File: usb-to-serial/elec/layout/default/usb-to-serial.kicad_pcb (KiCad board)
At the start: 2 copper layers, 225.7 x 100.8 mm, 0 parts

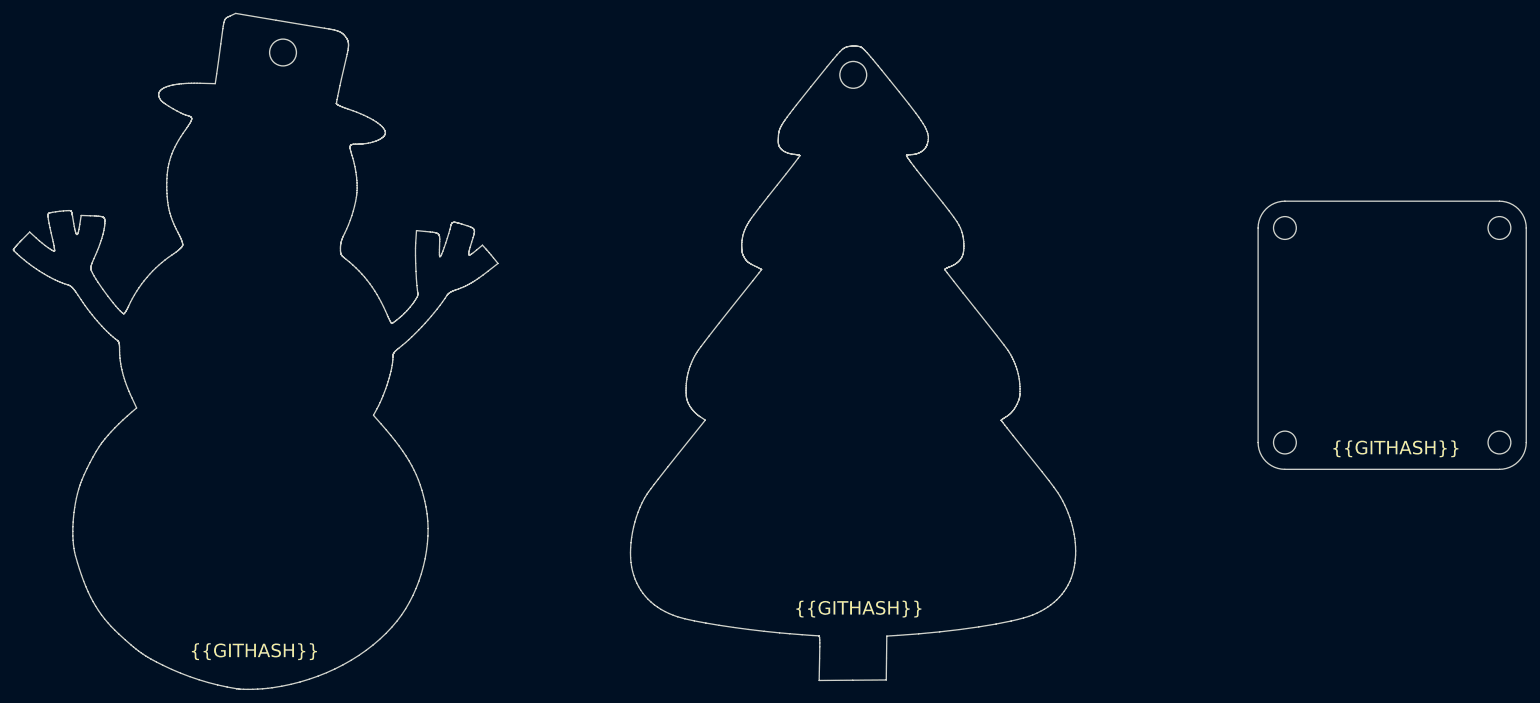
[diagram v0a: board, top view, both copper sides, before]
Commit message: updated usb to serial dev module, connected traces
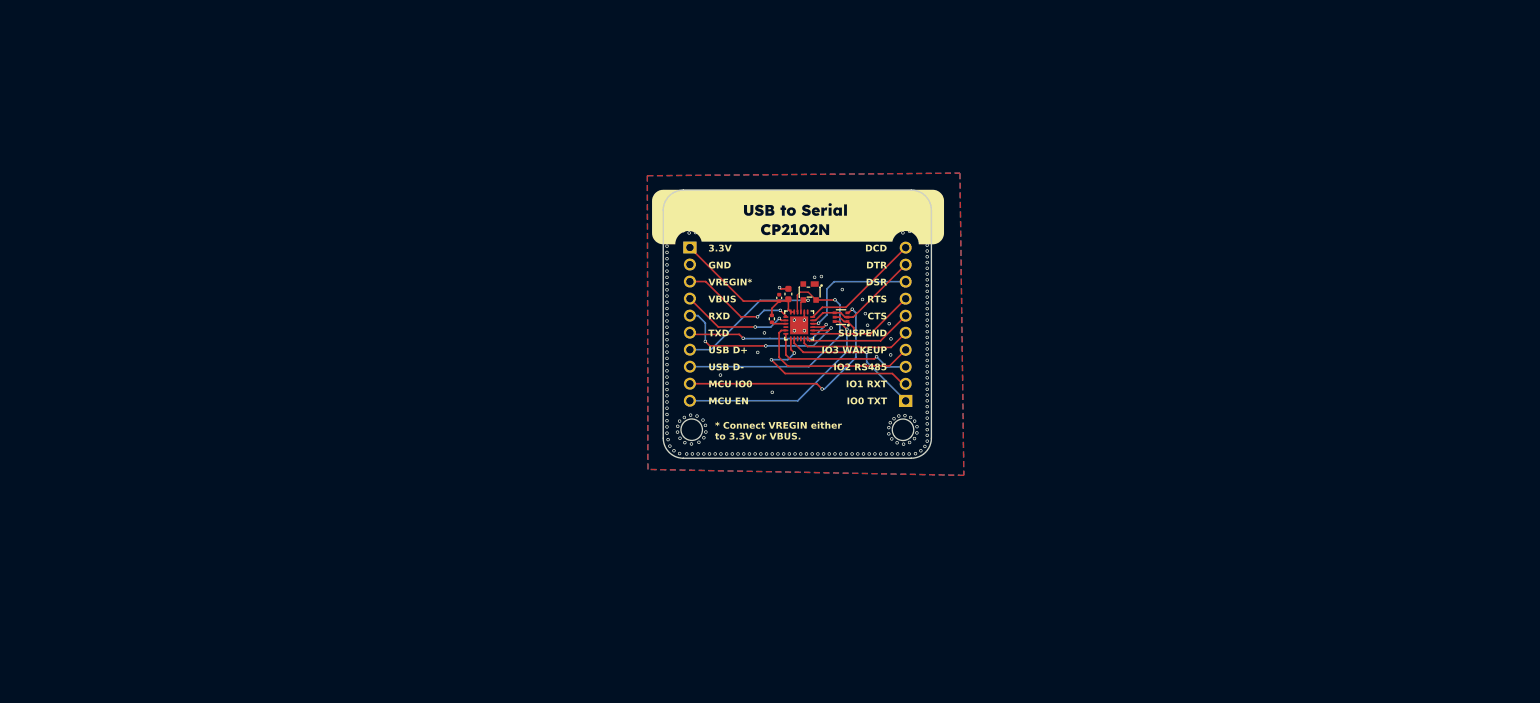
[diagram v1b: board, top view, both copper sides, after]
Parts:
- added C1: 16V 100nF X7R ±10% 0402 Multilayer Ceramic Capacitors MLCC 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, lib:C0402, F.Cu at (150.2, 92.2)
- added C2: 10V 10uF X5R ±10% 0603 Multilayer Ceramic Capacitors MLCC -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, lib:C0603, F.Cu at (151.6, 91.6)
- added R1: 62.5mW Thick Film Resistors 50V ±100ppm/℃ ±1% 1kΩ 0402 Chip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, lib:R0402, F.Cu at (149.1, 95.3)
- added REF**: OSHW-Logo2_7.3x6mm_SilkScreen, Symbol:OSHW-Logo2_7.3x6mm_SilkScreen, B.Cu at (144.4, 103.5)
- added U1: , lib:SOT-143-4_L2.9-W1.3-P1.92-LS2.4-BL, F.Cu at (154.7, 91.3)
- added U2: , lib:SC-70-6_L2.2-W1.3-P0.65-LS2.1-BR, F.Cu at (159.4, 95.1)
- added U3: , lib:QFN-24_L4.0-W4.0-P0.50-TL-EP2.6, F.Cu at (153.2, 96.3)
- added U4: , lib:CONN-TH_10P-P2.54_MX128-2.54-10P-GN01-CU-Y-A, F.Cu at (136.9, 96.1)
- added U5: , lib:CONN-TH_10P-P2.54_MX128-2.54-10P-GN01-CU-Y-A, F.Cu at (169.1, 96.2)
- added U6: , lib:MountingHole_3.2mm_M3, F.Cu at (137.1, 111.9)
- added U7: , lib:MountingHole_3.2mm_M3, F.Cu at (168.6, 80.4)
- added U8: , lib:MountingHole_3.2mm_M3, F.Cu at (137.1, 80.4)
- added U9: , lib:MountingHole_3.2mm_M3, F.Cu at (168.7, 111.9)
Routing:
- net dminus: track 0.00 -> 38.8 mm, vias 0 -> 1
- net mcu_io0: track 0.00 -> 35.4 mm, vias 0 -> 2
- net mcu_en: track 0.00 -> 32.1 mm, vias 0 -> 1
- net rxd: track 0.00 -> 28.6 mm, vias 0 -> 3
- net gpio_1_rxt: track 0.00 -> 27.7 mm, vias 0 -> 2
- net gpio_3_wakeup: track 0.00 -> 25.3 mm
- net txd: track 0.00 -> 23.7 mm, vias 0 -> 2
- net dplus: track 0.00 -> 23.3 mm, vias 0 -> 1
- net vio: track 0.00 -> 23.3 mm
- net gpio_2_rs485: track 0.00 -> 22.0 mm, vias 0 -> 1
- net gpio_0_txt: track 0.00 -> 21.7 mm, vias 0 -> 1
- net rts: track 0.00 -> 20.4 mm
- net dsr: track 0.00 -> 18.7 mm, vias 0 -> 1
- net dcd: track 0.00 -> 18.2 mm
- net dtr: track 0.00 -> 17.9 mm
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- added copper zone on B.Cu, net gnd
- added copper zone on F.Cu, net gnd
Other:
- board size 225.7 x 100.8 mm -> 40 x 40 mm
- board text added: "* Connect VREGIN either to 3.3V or VBUS."
- board text added: "3.3V"
- board text added: "CTS"
- board text added: "DCD"
- board text added: "DSR"
- board text added: "DTR"
- board text added: "GND"
- board text added: "IO0 TXT"
- board text added: "IO1 RXT"
- board text added: "IO2 RS485"
- board text added: "IO3 WAKEUP"
- board text added: "MCU EN"
- board text added: "MCU IO0"
- board text added: "RTS"
- board text added: "RXD"
- board text added: "SUSPEND"
- board text added: "Source files:"
- board text added: "TXD"
- board text added: "USB D+"
- board text added: "USB D-"
- board text added: "VBUS"
- board text added: "VREGIN*"
- board text added: "bit.ly/...."
- board text added: "designed by glowingkitty"
